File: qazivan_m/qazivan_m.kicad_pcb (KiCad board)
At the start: 2 copper layers, 204.9 x 76.2 mm, 97 parts, among them J1 AVR-ISP-6, J3 Conn_01x04_Female, U1 ATmega32U4-AU, Y1 16MHz

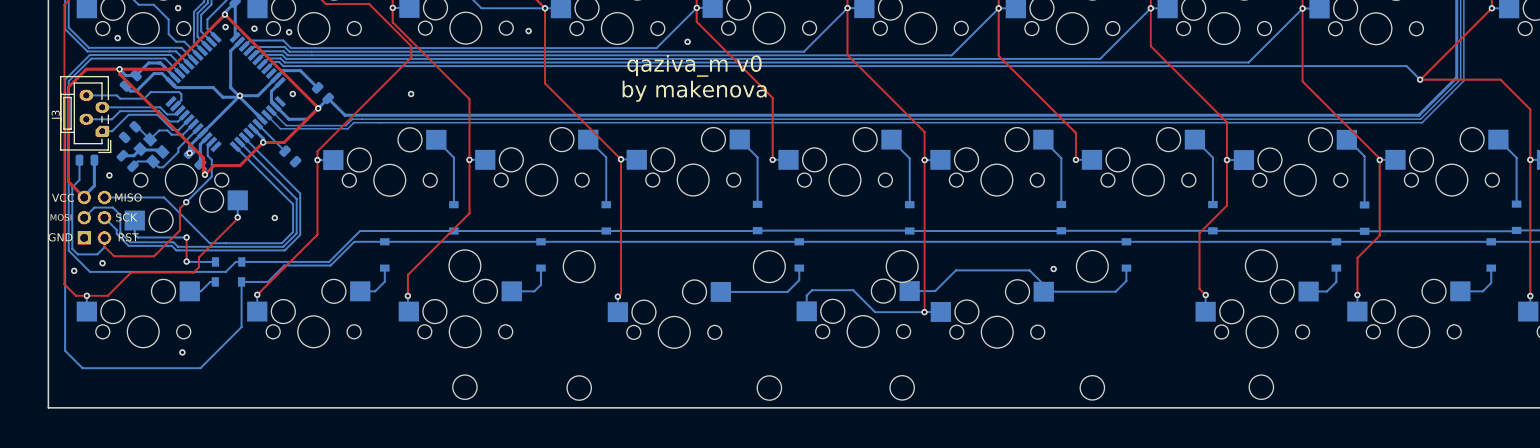
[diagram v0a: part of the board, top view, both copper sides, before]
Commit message: fixed bottom row, adding gamer row
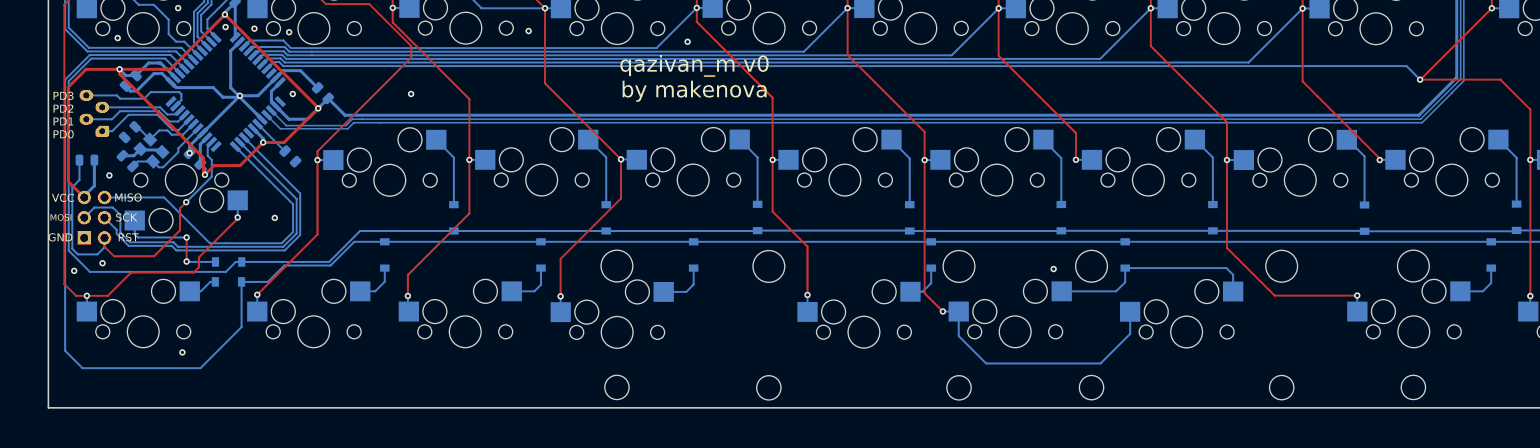
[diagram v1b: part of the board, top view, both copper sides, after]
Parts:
- MX33: footprint MX_Only:MXOnly-2.25U-Hotswap-ReversedStabilizers -> MX_Only:MXOnly-1U-Hotswap
- MX34: footprint MX_Only:MXOnly-2U-Hotswap-ReversedStabilizers -> MX_Only:MXOnly-2.25U-Hotswap-ReversedStabilizers
- MX35: footprint MX_Only:MXOnly-1U-Hotswap -> MX_Only:MXOnly-2U-Hotswap-ReversedStabilizers
- moved D35 26.5 mm to (170.6, 109.0)
- moved D34 24.5 mm to (146.2, 109.0)
- moved MX38 19.1 mm to (156.7, 118.6)
- moved MX34 16.7 mm to (137.8, 118.7)
- moved D33 13.3 mm to (116.4, 109.0)
- moved MX35 9.47 mm to (178.3, 118.7)
- moved MX33 7.17 mm to (106.8, 118.7)
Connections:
- MX34 pad 1: COL5 -> COL4
- MX35 pad 1: COL7 -> COL5
- MX36 pad 1: COL8 -> COL7
- MX38 pad 2: Net-(D34-Pad2) -> Net-(D35-Pad2)
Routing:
- net Net-(D34-Pad2): track 32.1 -> 4.94 mm
- net COL4: track 106.8 -> 127.7 mm, vias 3 -> 4
- net Net-(D35-Pad2): track 5.73 -> 26.2 mm
- net COL8: track 201.5 -> 181.3 mm, vias 4 -> 3
- net COL5: track 164.6 -> 177.5 mm
- net COL7: track 183.4 -> 194.5 mm
- net Net-(D33-Pad2): track 12.0 -> 6.22 mm
- net COL3: track 124.4 -> 127.3 mm
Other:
- board text added: "PD3 PD2 PD1 PD0"
- board text added: "qazivan_m v0 by makenova"
- board text removed: "qaziva_m v0 by makenova"

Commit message: updates
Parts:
- added D40: D_Small, Diode_SMD:D_SOD-123, B.Cu at (60.3, 47.1)
- added D41: D_Small, Diode_SMD:D_SOD-123, B.Cu at (79.4, 47.1)
- added D42: D_Small, Diode_SMD:D_SOD-123, B.Cu at (98.5, 47.1)
- added D43: D_Small, Diode_SMD:D_SOD-123, B.Cu at (117.5, 47.1)
- added D44: D_Small, Diode_SMD:D_SOD-123, B.Cu at (136.6, 47.1)
- added D45: D_Small, Diode_SMD:D_SOD-123, B.Cu at (155.5, 47.1)
- added MX40: MX-NoLED, MX_Only:MXOnly-1U-Hotswap, F.Cu at (54.4, 42.5)
- added MX41: MX-NoLED, MX_Only:MXOnly-1U-Hotswap, F.Cu at (73.5, 42.5)
- added MX42: MX-NoLED, MX_Only:MXOnly-1U-Hotswap, F.Cu at (92.5, 42.5)
- added MX43: MX-NoLED, MX_Only:MXOnly-1U-Hotswap, F.Cu at (111.6, 42.5)
- added MX44: MX-NoLED, MX_Only:MXOnly-1U-Hotswap, F.Cu at (130.6, 42.5)
- added MX45: MX-NoLED, MX_Only:MXOnly-1U-Hotswap, F.Cu at (149.7, 42.5)
- added REF**: breakaway-mousebites, random-keyboard-parts:breakaway-mousebites, F.Cu at (111.6, 52.2)
- added REF**: breakaway-mousebites, random-keyboard-parts:breakaway-mousebites, F.Cu at (149.8, 52.2)
- added REF**: breakaway-mousebites, random-keyboard-parts:breakaway-mousebites, F.Cu at (73.6, 52.2)
- added REF**: breakaway-mousebites, random-keyboard-parts:breakaway-mousebites, F.Cu at (92.6, 52.2)
- added REF**: breakaway-mousebites, random-keyboard-parts:breakaway-mousebites, F.Cu at (54.5, 52.2)
- added REF**: breakaway-mousebites, random-keyboard-parts:breakaway-mousebites, F.Cu at (130.8, 52.2)
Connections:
- U1 pad 22: unconnected-(U1-Pad22) -> ROW2
- U1 pad 25: ROW2 -> ROW3
- U1 pad 26: ROW3 -> ROW4
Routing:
- net ROW4: track 0.00 -> 160.5 mm
- net COL6: track 143.8 -> 166.8 mm, vias 3 -> 5
- net COL3: track 127.3 -> 150.4 mm, vias 4 -> 6
- net COL2: track 112.0 -> 135.0 mm, vias 4 -> 6
- net COL4: track 127.7 -> 150.7 mm, vias 4 -> 6
- net COL1: track 103.5 -> 126.5 mm, vias 4 -> 6
- net COL5: track 177.5 -> 200.5 mm, vias 4 -> 6
- net Net-(D41-Pad2): track 0.00 -> 9.01 mm
- net Net-(D42-Pad2): track 0.00 -> 9.00 mm
- net Net-(D43-Pad2): track 0.00 -> 8.97 mm
- net Net-(D45-Pad2): track 0.00 -> 8.94 mm
- net Net-(D40-Pad2): track 0.00 -> 8.89 mm
- net Net-(D44-Pad2): track 0.00 -> 8.84 mm
- net +5V: track 295.9 -> 301.2 mm
- net ROW2: track 236.2 -> 234.5 mm
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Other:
- board size 204.9 x 76.2 mm -> 204.8 x 95.2 mm
- board text added: "qaziv4n_m v0 by makenova"
- board text removed: "qazivan_m v0 by makenova"

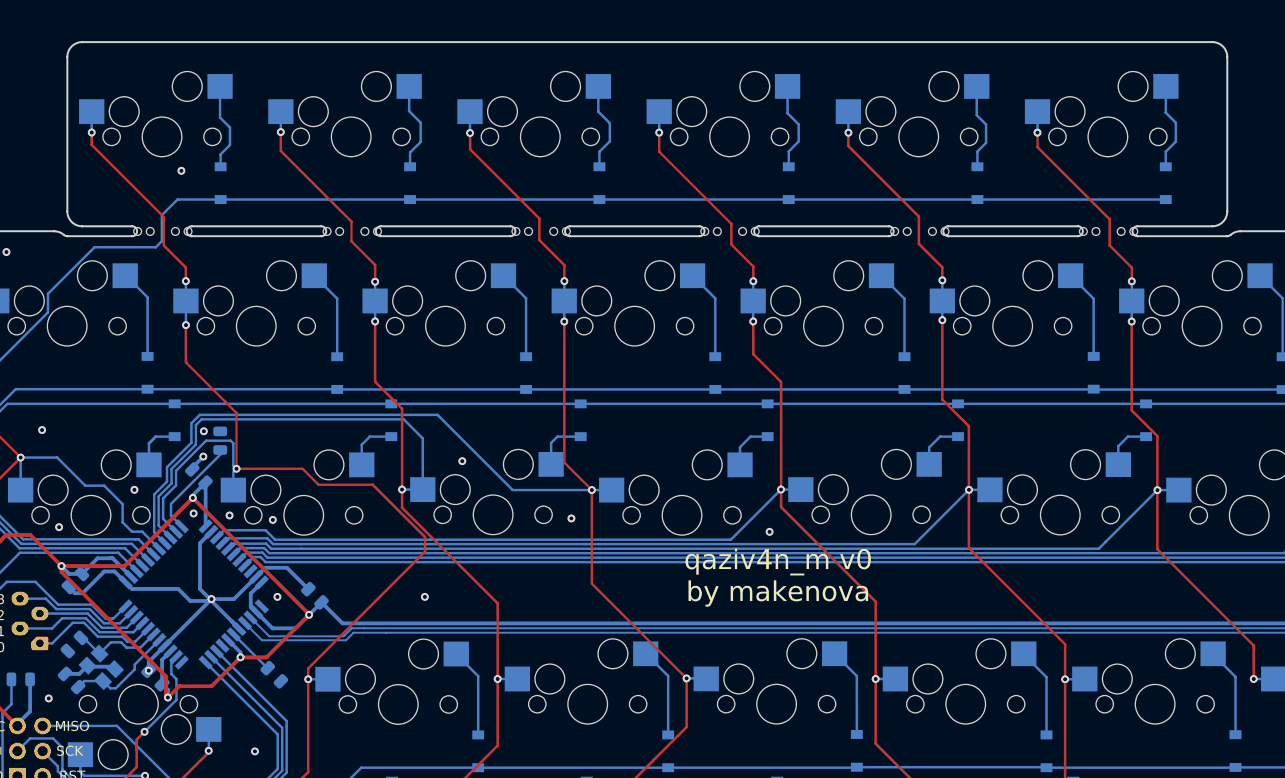
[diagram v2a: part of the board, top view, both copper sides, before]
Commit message: add indicator leds. need to figure out mouting
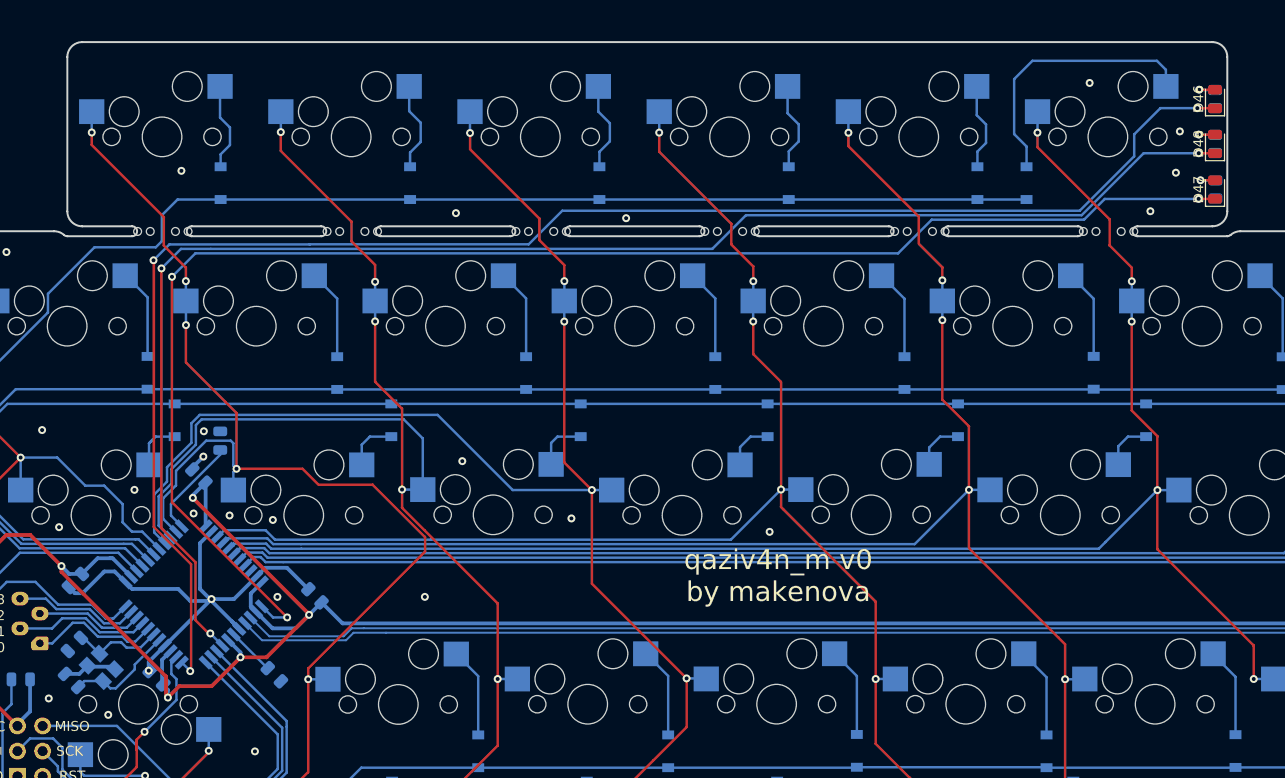
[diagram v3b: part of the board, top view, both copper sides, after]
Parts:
- added D46: LED, LED_SMD:LED_0805_2012Metric, F.Cu at (160.5, 38.7)
- added D47: LED, LED_SMD:LED_0805_2012Metric, F.Cu at (160.5, 47.8)
- added D48: LED, LED_SMD:LED_0805_2012Metric, F.Cu at (160.5, 43.2)
- added R7: 500, Resistor_SMD:R_0805_2012Metric, B.Cu at (160.5, 38.7)
- added R8: 500, Resistor_SMD:R_0805_2012Metric, B.Cu at (160.5, 47.8)
- added R9: 500, Resistor_SMD:R_0805_2012Metric, B.Cu at (160.5, 43.2)
- moved D45 14.0 mm to (141.5, 47.1)
- moved C6 0.12 mm to (53.9, 96.9)
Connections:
- U1 pad 1: unconnected-(U1-Pad1) -> LED2
- U1 pad 12: unconnected-(U1-Pad12) -> LED1
- U1 pad 8: unconnected-(U1-Pad8) -> LED3
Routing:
- net LED1: track 0.00 -> 158.8 mm, vias 0 -> 3
- net LED3: track 0.00 -> 151.6 mm, vias 0 -> 3
- net LED2: track 0.00 -> 150.4 mm, vias 0 -> 3
- net Net-(D45-Pad2): track 8.94 -> 27.4 mm
- net +5V: track 301.2 -> 285.1 mm
- net ROW4: track 160.5 -> 146.5 mm
- net Net-(D48-Pad2): track 0.00 -> 3.30 mm, vias 0 -> 1
- net Net-(R7-Pad1): track 0.00 -> 3.22 mm, vias 0 -> 1
- net Net-(D47-Pad2): track 0.00 -> 2.96 mm, vias 0 -> 1
- net GND: vias 25 -> 32

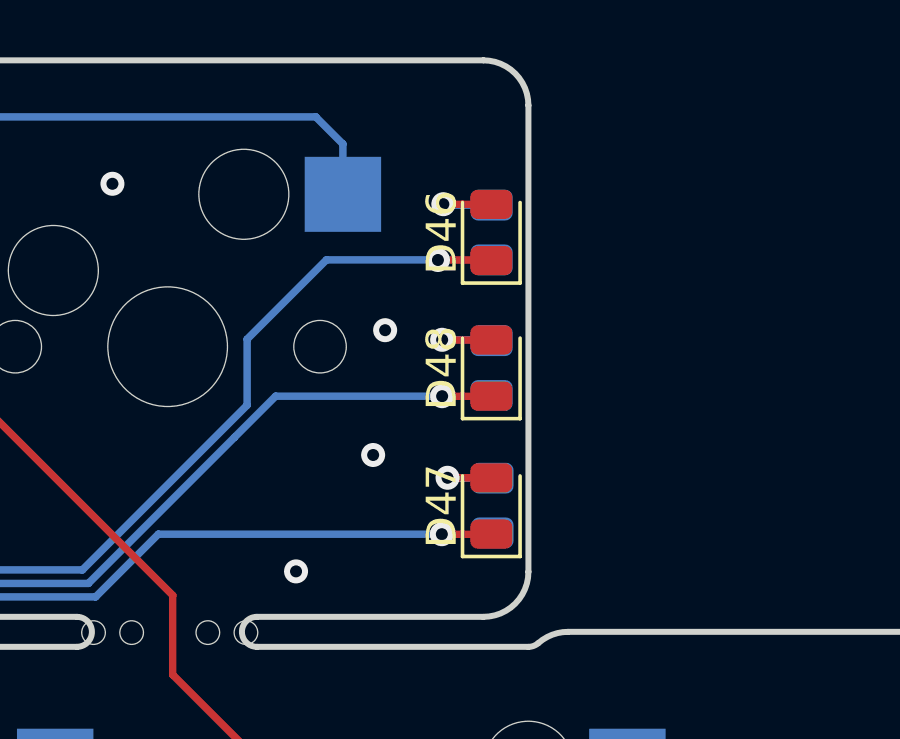
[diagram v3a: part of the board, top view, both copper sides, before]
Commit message: fix indicator leds
mcu pin to anode not cathode
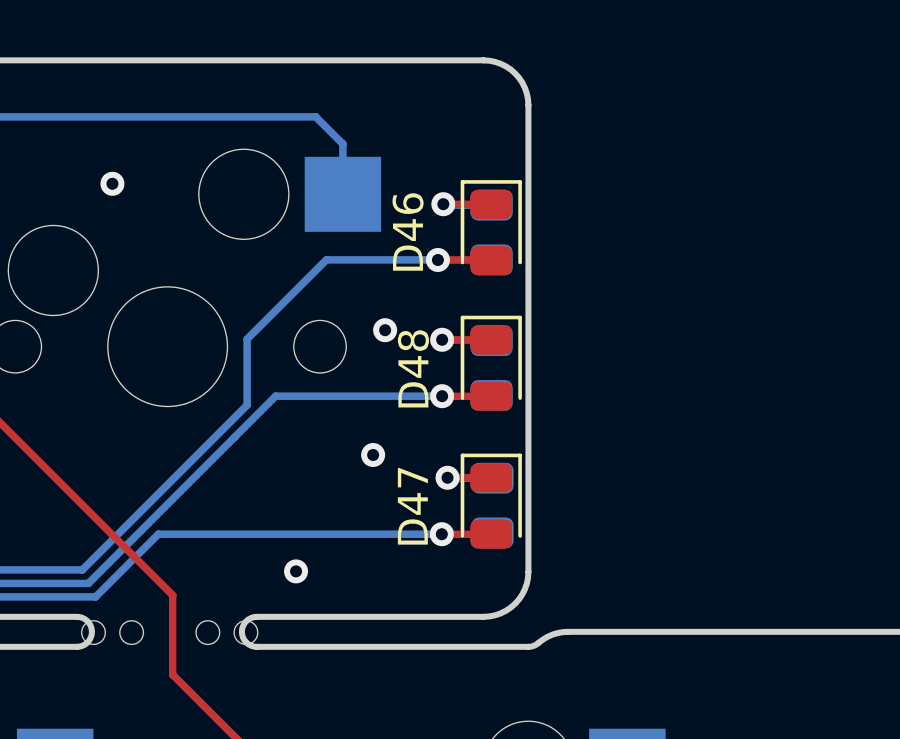
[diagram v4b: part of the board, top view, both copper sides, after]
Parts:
- turned D46 to -90 degrees
- turned D47 to -90 degrees
- turned D48 to -90 degrees
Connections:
- D46 pad 1: LED1 -> Net-(R7-Pad1)
- D46 pad 2: Net-(R7-Pad1) -> LED1
- D47 pad 1: LED2 -> Net-(R8-Pad1)
- D47 pad 2: Net-(D47-Pad2) -> LED2
- D48 pad 1: LED3 -> Net-(R9-Pad1)
- D48 pad 2: Net-(D48-Pad2) -> LED3
- R8 pad 1: Net-(D47-Pad2) -> Net-(R8-Pad1)
- R9 pad 1: Net-(D48-Pad2) -> Net-(R9-Pad1)
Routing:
- net Net-(R9-Pad1): track 0.00 -> 3.30 mm, vias 0 -> 1
- net Net-(D48-Pad2): track 3.30 -> 0.00 mm, vias 1 -> 0
- net Net-(R8-Pad1): track 0.00 -> 2.96 mm, vias 0 -> 1
- net Net-(D47-Pad2): track 2.96 -> 0.00 mm, vias 1 -> 0
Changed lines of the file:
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@@
   (net 83 "Net-(D29-Pad2)")
   (net 84 "Net-(R7-Pad1)")
-  (net 85 "Net-(D47-Pad2)")
-  (net 86 "Net-(D48-Pad2)")
+  (net 85 "Net-(R8-Pad1)")
+  (net 86 "Net-(R9-Pad1)")
   (net 87 "LED1")
   (net 88 "LED2")
@@
   )
   (footprint "LED_SMD:LED_0805_2012Metric" (layer "F.Cu")
-    (at 160.479026 43.172734 90)
+    (at 160.479026 43.172734 -90)
     (descr "LED SMD 0805 (2012 Metric), square (rectangular) end terminal, IPC_7351 nominal, (Body size source: https://docs.google.com/spreadsheets/d/1BsfQQcO9C6DZCsRaXUlFlo91Tg2WpOkGARC1WS5S8t0/edit?usp=sharing), generated with kicad-footprint-generator")
     (tags "LED")
@@
     (property "Sheetname" "")
     (attr smd)
-    (fp_text reference "D48" (at 0 -1.65 90) (layer "F.SilkS")
+    (fp_text reference "D48" (at 0.047266 2.559026 90) (layer "F.SilkS")
       (effects (font (size 1 1) (thickness 0.15)))
     )
@@
     (fp_line (start 1 -0.6) (end -0.7 -0.6) (layer "F.Fab") (width 0.1))
     (fp_line (start -1 -0.3) (end -1 0.6) (layer "F.Fab") (width 0.1))
-    (pad "1" smd roundrect (at -0.9375 0 90) (size 0.975 1.4) (layers "F.Cu" "F.Paste" "F.Mask") (roundrect_rratio 0.25)
-      (net 89 "LED3") (pinfunction "K") (pintype "passive"))
-    (pad "2" smd roundrect (at 0.9375 0 90) (size 0.975 1.4) (layers "F.Cu" "F.Paste" "F.Mask") (roundrect_rratio 0.25)
-      (net 86 "Net-(D48-Pad2)") (pinfunction "A") (pintype "passive"))
+    (pad "1" smd roundrect (at -0.9375 0 270) (size 0.975 1.4) (layers "F.Cu" "F.Paste" "F.Mask") (roundrect_rratio 0.25)
+      (net 86 "Net-(R9-Pad1)") (pinfunction "K") (pintype "passive"))
+    (pad "2" smd roundrect (at 0.9375 0 270) (size 0.975 1.4) (layers "F.Cu" "F.Paste" "F.Mask") (roundrect_rratio 0.25)
+      (net 89 "LED3") (pinfunction "A") (pintype "passive"))
     (model "${KICAD6_3DMODEL_DIR}/LED_SMD.3dshapes/LED_0805_2012Metric.wrl"
       (offset (xyz 0 0 0))
@@
   )
   (footprint "LED_SMD:LED_0805_2012Metric" (layer "F.Cu")
-    (at 160.479026 38.653593 90)
+    (at 160.479026 38.653593 -90)
     (descr "LED SMD 0805 (2012 Metric), square (rectangular) end terminal, IPC_7351 nominal, (Body size source: https://docs.google.com/spreadsheets/d/1BsfQQcO9C6DZCsRaXUlFlo91Tg2WpOkGARC1WS5S8t0/edit?usp=sharing), generated with kicad-footprint-generator")
     (tags "LED")
@@
     (property "Sheetname" "")
     (attr smd)
-    (fp_text reference "D46" (at 0 -1.65 90) (layer "F.SilkS")
+    (fp_text reference "D46" (at 0.006407 2.739026 90) (layer "F.SilkS")
       (effects (font (size 1 1) (thickness 0.15)))
     )
@@
     (fp_line (start -1 0.6) (end 1 0.6) (layer "F.Fab") (width 0.1))
     (fp_line (start -0.7 -0.6) (end -1 -0.3) (layer "F.Fab") (width 0.1))
-    (pad "1" smd roundrect (at -0.9375 0 90) (size 0.975 1.4) (layers "F.Cu" "F.Paste" "F.Mask") (roundrect_rratio 0.25)
-      (net 87 "LED1") (pinfunction "K") (pintype "passive"))
-    (pad "2" smd roundrect (at 0.9375 0 90) (size 0.975 1.4) (layers "F.Cu" "F.Paste" "F.Mask") (roundrect_rratio 0.25)
-      (net 84 "Net-(R7-Pad1)") (pinfunction "A") (pintype "passive"))
+    (pad "1" smd roundrect (at -0.9375 0 270) (size 0.975 1.4) (layers "F.Cu" "F.Paste" "F.Mask") (roundrect_rratio 0.25)
+      (net 84 "Net-(R7-Pad1)") (pinfunction "K") (pintype "passive"))
+    (pad "2" smd roundrect (at 0.9375 0 270) (size 0.975 1.4) (layers "F.Cu" "F.Paste" "F.Mask") (roundrect_rratio 0.25)
+      (net 87 "LED1") (pinfunction "A") (pintype "passive"))
     (model "${KICAD6_3DMODEL_DIR}/LED_SMD.3dshapes/LED_0805_2012Metric.wrl"
       (offset (xyz 0 0 0))
@@
   )
   (footprint "LED_SMD:LED_0805_2012Metric" (layer "F.Cu")
-    (at 160.479026 47.769231 90)
+    (at 160.479026 47.769231 -90)
     (descr "LED SMD 0805 (2012 Metric), square (rectangular) end terminal, IPC_7351 nominal, (Body size source: https://docs.google.com/spreadsheets/d/1BsfQQcO9C6DZCsRaXUlFlo91Tg2WpOkGARC1WS5S8t0/edit?usp=sharing), generated with kicad-footprint-generator")
     (tags "LED")
@@
     (property "Sheetname" "")
     (attr smd)
-    (fp_text reference "D47" (at 0 -1.65 90) (layer "F.SilkS")
+    (fp_text reference "D47" (at 0.020769 2.579026 90) (layer "F.SilkS")
       (effects (font (size 1 1) (thickness 0.15)))
     )
@@
     (fp_line (start -1 0.6) (end 1 0.6) (layer "F.Fab") (width 0.1))
     (fp_line (start -0.7 -0.6) (end -1 -0.3) (layer "F.Fab") (width 0.1))
-    (pad "1" smd roundrect (at -0.9375 0 90) (size 0.975 1.4) (layers "F.Cu" "F.Paste" "F.Mask") (roundrect_rratio 0.25)
-      (net 88 "LED2") (pinfunction "K") (pintype "passive"))
-    (pad "2" smd roundrect (at 0.9375 0 90) (size 0.975 1.4) (layers "F.Cu" "F.Paste" "F.Mask") (roundrect_rratio 0.25)
-      (net 85 "Net-(D47-Pad2)") (pinfunction "A") (pintype "passive"))
+    (pad "1" smd roundrect (at -0.9375 0 270) (size 0.975 1.4) (layers "F.Cu" "F.Paste" "F.Mask") (roundrect_rratio 0.25)
+      (net 85 "Net-(R8-Pad1)") (pinfunction "K") (pintype "passive"))
+    (pad "2" smd roundrect (at 0.9375 0 270) (size 0.975 1.4) (layers "F.Cu" "F.Paste" "F.Mask") (roundrect_rratio 0.25)
+      (net 88 "LED2") (pinfunction "A") (pintype "passive"))
     (model "${KICAD6_3DMODEL_DIR}/LED_SMD.3dshapes/LED_0805_2012Metric.wrl"
       (offset (xyz 0 0 0))
@@
     (fp_line (start -1 -0.625) (end -1 0.625) (layer "B.Fab") (width 0.1))
     (pad "1" smd roundrect (at -0.9125 0 270) (size 1.025 1.4) (layers "B.Cu" "B.Paste" "B.Mask") (roundrect_rratio 0.243902)
-      (net 86 "Net-(D48-Pad2)") (pintype "passive"))
+      (net 86 "Net-(R9-Pad1)") (pintype "passive"))
     (pad "2" smd roundrect (at 0.9125 0 270) (size 1.025 1.4) (layers "B.Cu" "B.Paste" "B.Mask") (roundrect_rratio 0.243902)
       (net 1 "GND") (pintype "passive"))
@@
     (fp_line (start -1 0.625) (end 1 0.625) (layer "B.Fab") (width 0.1))
     (pad "1" smd roundrect (at -0.9125 0 270) (size 1.025 1.4) (layers "B.Cu" "B.Paste" "B.Mask") (roundrect_rratio 0.243902)
-      (net 85 "Net-(D47-Pad2)") (pintype "passive"))
+      (net 85 "Net-(R8-Pad1)") (pintype "passive"))
     (pad "2" smd roundrect (at 0.9125 0 270) (size 1.025 1.4) (layers "B.Cu" "B.Paste" "B.Mask") (roundrect_rratio 0.243902)
       (net 1 "GND") (pintype "passive"))
